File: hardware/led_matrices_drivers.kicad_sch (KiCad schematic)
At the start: 12 parts, among them U6 MAX7219, U7 MAX7219, U8 MAX7219, U9 MAX7219

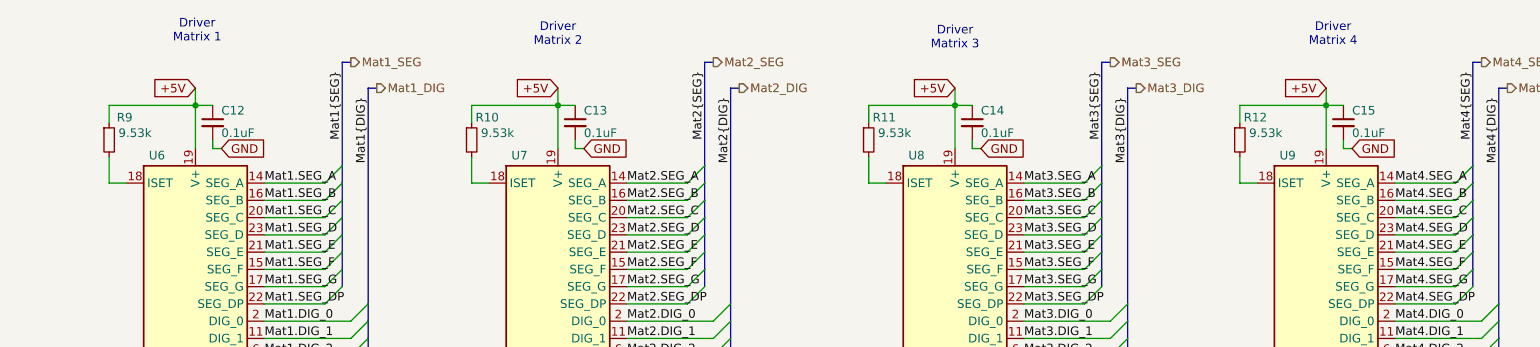
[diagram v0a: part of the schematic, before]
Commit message: Added the LED Matrice Display schematic. Added LED Matrix symbol
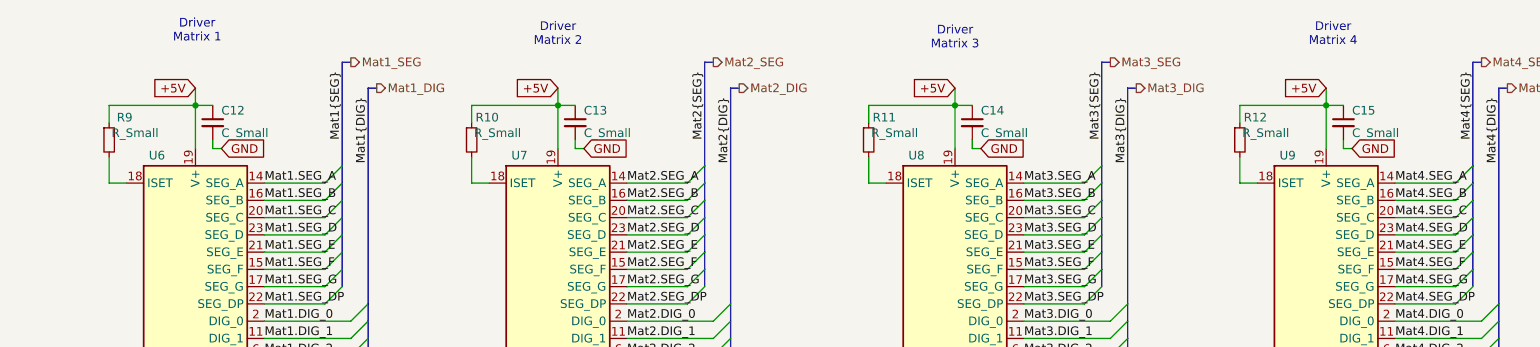
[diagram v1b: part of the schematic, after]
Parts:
- C12, C13, C14, C15: value 0.1uF -> C_Small
- R10, R11, R12, R9: value 9.53k -> R_Small
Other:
- title: Kitchen_Timer -> Kitchen_Timer: LED Matrices Drivers
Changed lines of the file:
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@@
 	(paper "A4")
 	(title_block
-		(title "Kitchen_Timer")
+		(title "Kitchen_Timer: LED Matrices Drivers")
 		(date "2025-01-25")
-		(rev "V01")
+		(rev "v01")
 	)
 	(bus_alias "DIG"
@@
 			)
 		)
-		(property "Value" "9.53k"
+		(property "Value" "R_Small"
 			(at 166.37 66.294 0)
 			(effects
@@
 			)
 		)
-		(property "Value" "9.53k"
+		(property "Value" "R_Small"
 			(at 107.95 66.294 0)
 			(effects
@@
 			)
 		)
-		(property "Value" "9.53k"
+		(property "Value" "R_Small"
 			(at 54.61 66.294 0)
 			(effects
@@
 			)
 		)
-		(property "Value" "0.1uF"
+		(property "Value" "C_Small"
 			(at 233.68 66.294 0)
 			(effects
@@
 			)
 		)
-		(property "Value" "0.1uF"
+		(property "Value" "C_Small"
 			(at 179.07 66.294 0)
 			(effects
@@
 			)
 		)
-		(property "Value" "0.1uF"
+		(property "Value" "C_Small"
 			(at 120.65 66.294 0)
 			(effects
@@
 			)
 		)
-		(property "Value" "0.1uF"
+		(property "Value" "C_Small"
 			(at 67.31 66.294 0)
 			(effects
@@
 			)
 		)
-		(property "Value" "9.53k"
+		(property "Value" "R_Small"
 			(at 220.98 66.294 0)
 			(effects

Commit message: Added the values of resostors and caps that for some reason got reseted.
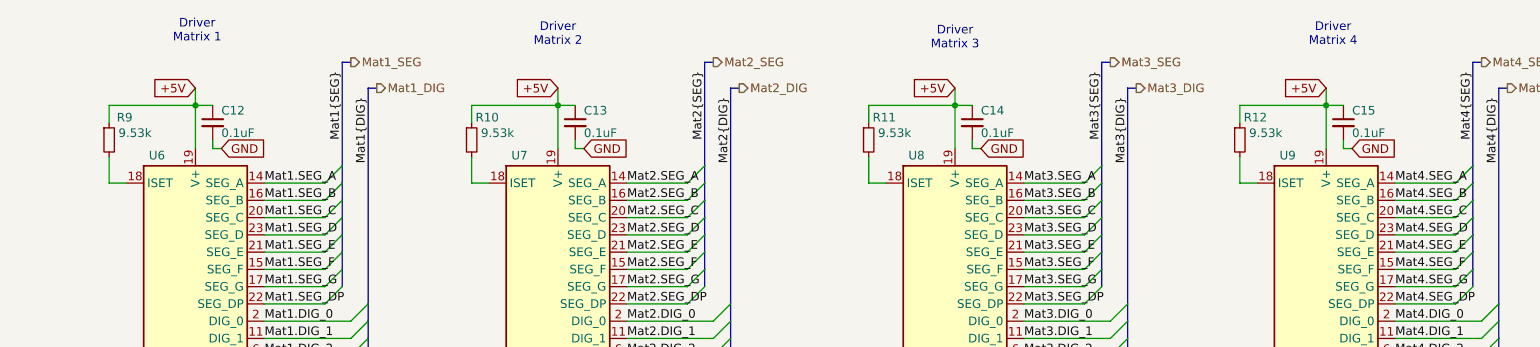
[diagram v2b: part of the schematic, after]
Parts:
- C12, C13, C14, C15: value C_Small -> 0.1uF
- R10, R11, R12, R9: value R_Small -> 9.53k
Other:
- title: Kitchen_Timer: LED Matrices Drivers -> Kitchen_Timer - LED Matrices Drivers
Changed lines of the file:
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@@
 	(paper "A4")
 	(title_block
-		(title "Kitchen_Timer: LED Matrices Drivers")
+		(title "Kitchen_Timer - LED Matrices Drivers")
 		(date "2025-01-25")
 		(rev "v01")
+		(comment 2 "creativecommons.org/licences/4.0/")
+		(comment 3 "Licence: CC BY 4.0")
+		(comment 4 "Author: Nicolas Perozzi")
 	)
 	(bus_alias "DIG"
@@
 			)
 		)
-		(property "Value" "R_Small"
+		(property "Value" "9.53k"
 			(at 166.37 66.294 0)
 			(effects
@@
 			)
 		)
-		(property "Value" "R_Small"
+		(property "Value" "9.53k"
 			(at 107.95 66.294 0)
 			(effects
@@
 			)
 		)
-		(property "Value" "R_Small"
+		(property "Value" "9.53k"
 			(at 54.61 66.294 0)
 			(effects
@@
 			)
 		)
-		(property "Value" "C_Small"
+		(property "Value" "0.1uF"
 			(at 233.68 66.294 0)
 			(effects
@@
 			)
 		)
-		(property "Value" "C_Small"
+		(property "Value" "0.1uF"
 			(at 179.07 66.294 0)
 			(effects
@@
 			)
 		)
-		(property "Value" "C_Small"
+		(property "Value" "0.1uF"
 			(at 120.65 66.294 0)
 			(effects
@@
 			)
 		)
-		(property "Value" "C_Small"
+		(property "Value" "0.1uF"
 			(at 67.31 66.294 0)
 			(effects
@@
 			)
 		)
-		(property "Value" "R_Small"
+		(property "Value" "9.53k"
 			(at 220.98 66.294 0)
 			(effects

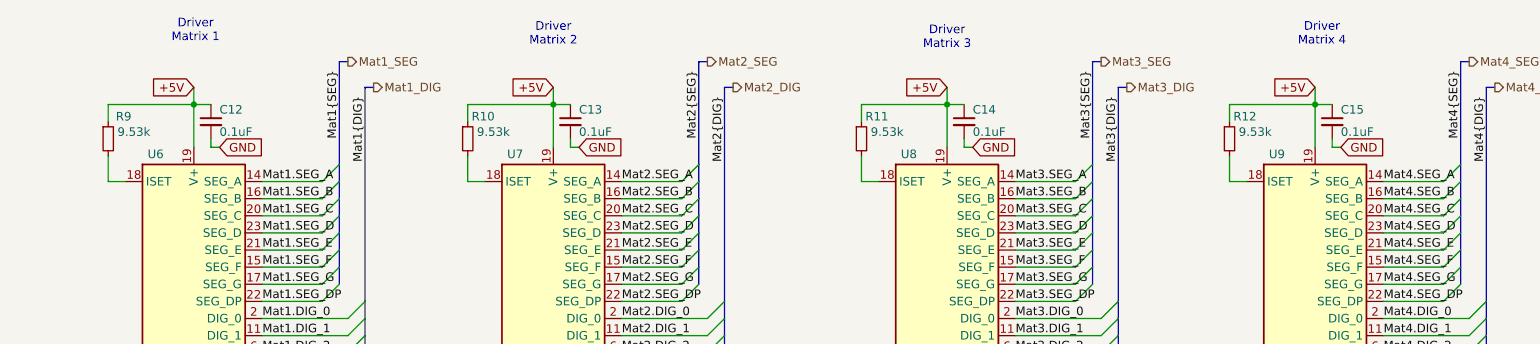
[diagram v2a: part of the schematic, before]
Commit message: Added data to the components table
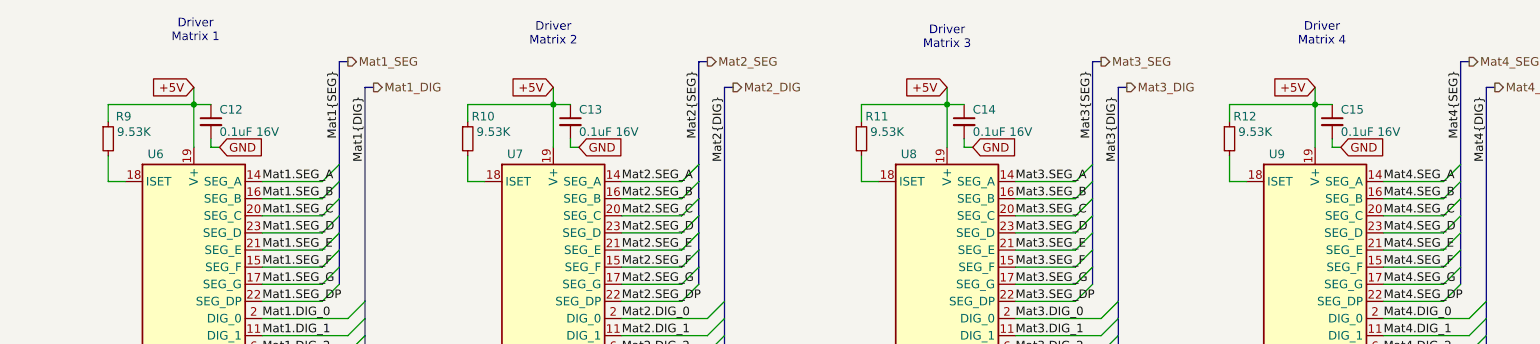
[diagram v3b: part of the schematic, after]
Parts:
- C12, C13, C14, C15: value 0.1uF -> 0.1uF 16V; Package (none) -> 0805; Part Num (none) -> GRM21BR71H104KA01L; Price/unit (none) -> $0.0097; Supplier Link (none) -> https://jlcpcb.com/partdetail/MurataElectronics-GRM21BR71H1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
- R10, R11, R12, R9: value 9.53k -> 9.53K; Package (none) -> 0805; Part Num (none) -> CR0805F89531G; Price/unit (none) -> $0.0022; Supplier Link (none) -> https://jlcpcb.com/partdetail/LizElec-CR0805F89531G/C101913
- U6, U7, U8, U9: Package (none) -> SOIC-24-300mil; Part Num (none) -> MAX7219CWG+T; Price/unit (none) -> $2.6325; Supplier Link (none) -> https://jlcpcb.com/partdetail/10499-MAX7219CWGT/C9964

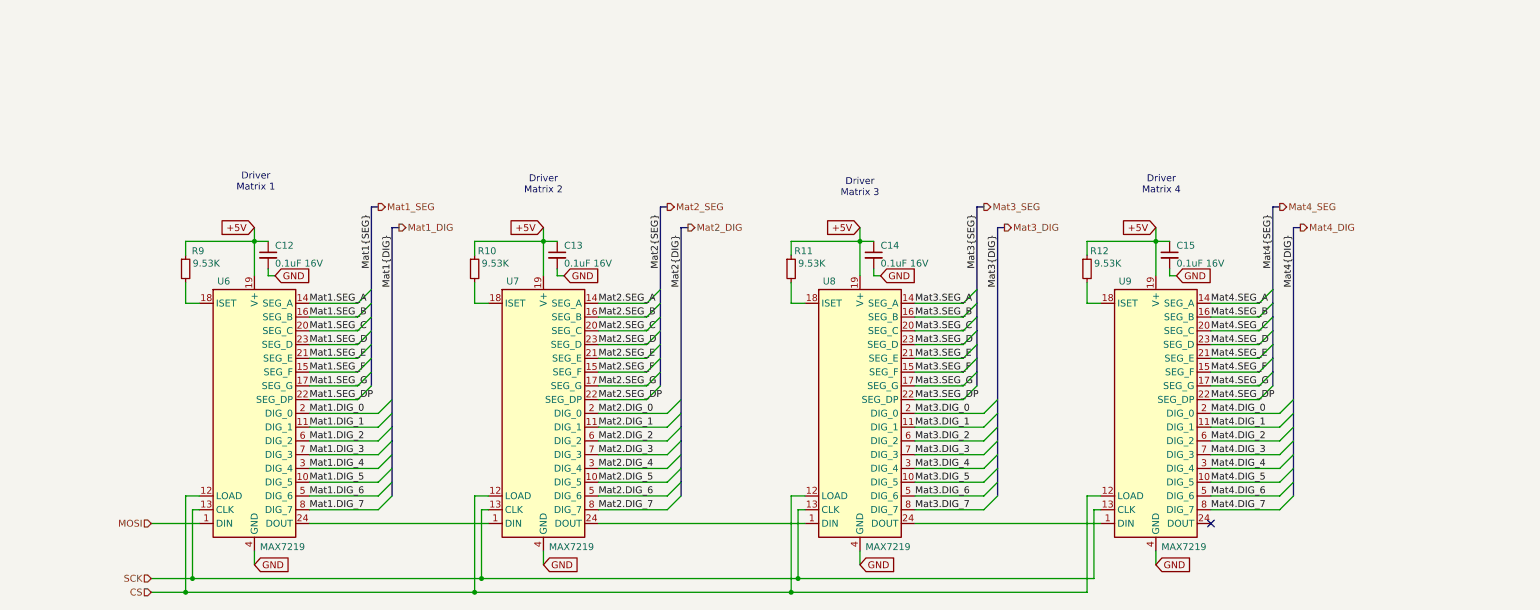
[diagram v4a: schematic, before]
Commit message: Schematic completed, commented and ready for review
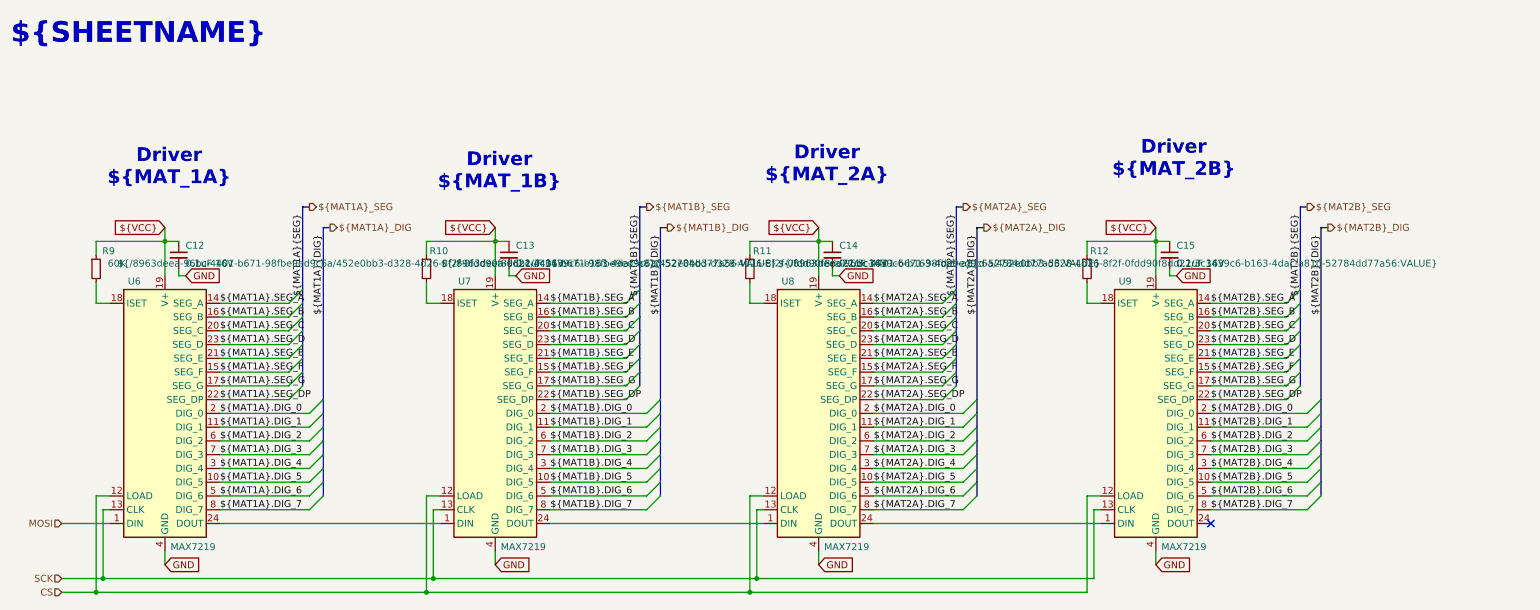
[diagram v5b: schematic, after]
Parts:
- R10, R11, R12: value 9.53K -> ${/8963deea-96bc-4401-b671-98fbe9ed9c6a/452e0bb3-d328-4d26-8f2f-0fdd90f8dd22/3c3439c6-b163-4dac-a81d-52784dd77a56:VALUE}; Supplier Link https://jlcpcb.com/partdetail/LizElec-CR0805F89531G/C101913 -> (none)
- R9: value 9.53K -> 60K; Supplier Link https://jlcpcb.com/partdetail/LizElec-CR0805F89531G/C101913 -> (none)
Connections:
- net +5V renamed ${VCC}
- net Mat1.DIG_0 renamed ${MAT1A}.DIG_0
- net Mat1.DIG_1 renamed ${MAT1A}.DIG_1
- net Mat1.DIG_2 renamed ${MAT1A}.DIG_2
- net Mat1.DIG_3 renamed ${MAT1A}.DIG_3
- net Mat1.DIG_4 renamed ${MAT1A}.DIG_4
- net Mat1.DIG_5 renamed ${MAT1A}.DIG_5
- net Mat1.DIG_6 renamed ${MAT1A}.DIG_6
- net Mat1.DIG_7 renamed ${MAT1A}.DIG_7
- net Mat1.SEG_A renamed ${MAT1A}.SEG_A
- net Mat1.SEG_B renamed ${MAT1A}.SEG_B
- net Mat1.SEG_C renamed ${MAT1A}.SEG_C
- net Mat1.SEG_D renamed ${MAT1A}.SEG_D
- net Mat1.SEG_DP renamed ${MAT1A}.SEG_DP
- net Mat1.SEG_E renamed ${MAT1A}.SEG_E
- net Mat1.SEG_F renamed ${MAT1A}.SEG_F
- net Mat1.SEG_G renamed ${MAT1A}.SEG_G
- net Mat2.DIG_0 renamed ${MAT1B}.DIG_0
- net Mat2.DIG_1 renamed ${MAT1B}.DIG_1
- net Mat2.DIG_2 renamed ${MAT1B}.DIG_2
- net Mat2.DIG_3 renamed ${MAT1B}.DIG_3
- net Mat2.DIG_4 renamed ${MAT1B}.DIG_4
- net Mat2.DIG_5 renamed ${MAT1B}.DIG_5
- net Mat2.DIG_6 renamed ${MAT1B}.DIG_6
- net Mat2.DIG_7 renamed ${MAT1B}.DIG_7
- net Mat2.SEG_A renamed ${MAT1B}.SEG_A
- net Mat2.SEG_B renamed ${MAT1B}.SEG_B
- net Mat2.SEG_C renamed ${MAT1B}.SEG_C
- net Mat2.SEG_D renamed ${MAT1B}.SEG_D
- net Mat2.SEG_DP renamed ${MAT1B}.SEG_DP
- net Mat2.SEG_E renamed ${MAT1B}.SEG_E
- net Mat2.SEG_F renamed ${MAT1B}.SEG_F
- net Mat2.SEG_G renamed ${MAT1B}.SEG_G
- net Mat3.DIG_0 renamed ${MAT2A}.DIG_0
- net Mat3.DIG_1 renamed ${MAT2A}.DIG_1
- net Mat3.DIG_2 renamed ${MAT2A}.DIG_2
- net Mat3.DIG_3 renamed ${MAT2A}.DIG_3
- net Mat3.DIG_4 renamed ${MAT2A}.DIG_4
- net Mat3.DIG_5 renamed ${MAT2A}.DIG_5
- net Mat3.DIG_6 renamed ${MAT2A}.DIG_6
- net Mat3.DIG_7 renamed ${MAT2A}.DIG_7
- net Mat3.SEG_A renamed ${MAT2A}.SEG_A
- net Mat3.SEG_B renamed ${MAT2A}.SEG_B
- net Mat3.SEG_C renamed ${MAT2A}.SEG_C
- net Mat3.SEG_D renamed ${MAT2A}.SEG_D
- net Mat3.SEG_DP renamed ${MAT2A}.SEG_DP
- net Mat3.SEG_E renamed ${MAT2A}.SEG_E
- net Mat3.SEG_F renamed ${MAT2A}.SEG_F
- net Mat3.SEG_G renamed ${MAT2A}.SEG_G
- net Mat4.DIG_0 renamed ${MAT2B}.DIG_0
- net Mat4.DIG_1 renamed ${MAT2B}.DIG_1
- net Mat4.DIG_2 renamed ${MAT2B}.DIG_2
- net Mat4.DIG_3 renamed ${MAT2B}.DIG_3
- net Mat4.DIG_4 renamed ${MAT2B}.DIG_4
- net Mat4.DIG_5 renamed ${MAT2B}.DIG_5
- net Mat4.DIG_6 renamed ${MAT2B}.DIG_6
- net Mat4.DIG_7 renamed ${MAT2B}.DIG_7
- net Mat4.SEG_A renamed ${MAT2B}.SEG_A
- net Mat4.SEG_B renamed ${MAT2B}.SEG_B
- net Mat4.SEG_C renamed ${MAT2B}.SEG_C
- net Mat4.SEG_D renamed ${MAT2B}.SEG_D
- net Mat4.SEG_DP renamed ${MAT2B}.SEG_DP
- net Mat4.SEG_E renamed ${MAT2B}.SEG_E
- net Mat4.SEG_F renamed ${MAT2B}.SEG_F
- net Mat4.SEG_G renamed ${MAT2B}.SEG_G
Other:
- note added: "${SHEETNAME}"
- note added: "Driver ${MAT_1A}"
- note added: "Driver ${MAT_1B}"
- note added: "Driver ${MAT_2A}"
- note added: "Driver ${MAT_2B}"
- note removed: "Driver Matrix 1"
- note removed: "Driver Matrix 2"
- note removed: "Driver Matrix 3"
- note removed: "Driver Matrix 4"
- title: Kitchen_Timer - LED Matrices Drivers -> Kitchen_Timer - ${SHEETNAME}
- moved on the sheet: C12, C13, C14, R10, R11, R9, U6, U7, U8
